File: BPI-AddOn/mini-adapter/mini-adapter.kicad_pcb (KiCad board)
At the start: 2 copper layers, 50 x 50 mm, 17 parts, among them J1 RJ45, J3 MS2 Kabel, J4 Grove, J5 RJ45, P1 DIN10-1, P2 DIN7-1, P3 CONN_01X05, P4 CAN Term

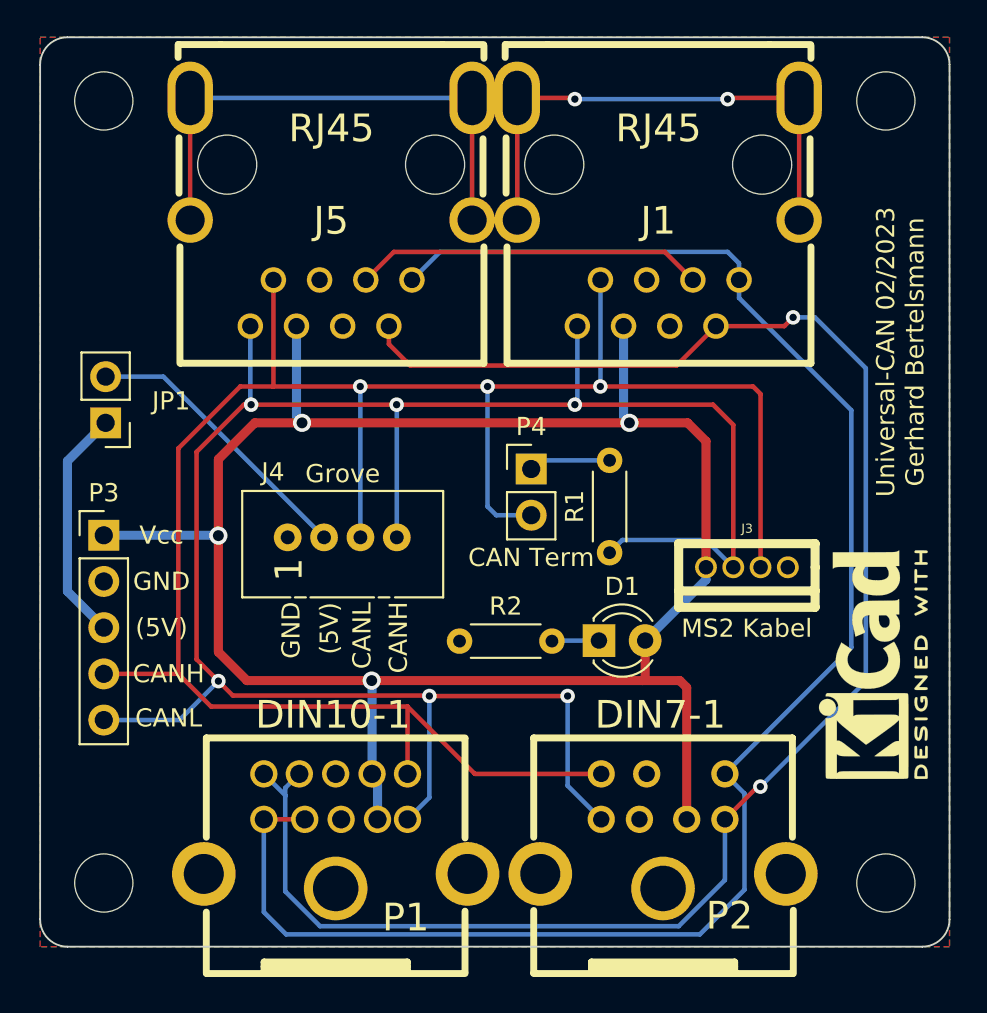
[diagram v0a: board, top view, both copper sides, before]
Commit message: add MS1 Slave / Pin 5 Vcc
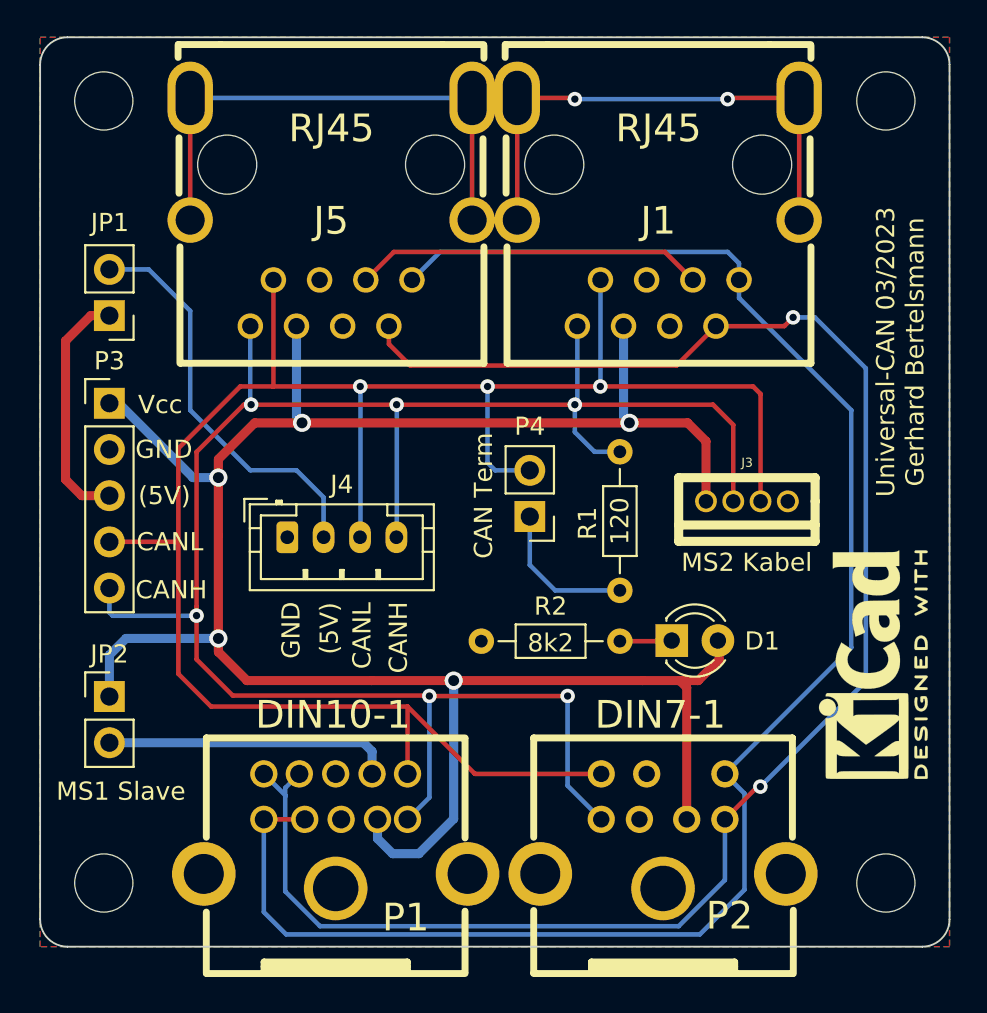
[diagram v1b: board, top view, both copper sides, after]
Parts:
- added JP2: MS1 Slave, Connector_PinHeader_2.54mm:PinHeader_1x02_P2.54mm_Vertical, F.Cu at (114.8, 111.2)
- J4: footprint Maerklin:Grove_1x04 -> Connector_JST:JST_PH_B4B-PH-K_1x04_P2.00mm_Vertical
- R1, R2: footprint Resistor_THT:R_Axial_DIN0204_L3.6mm_D1.6mm_P5.08mm_Horizontal -> Resistor_THT:R_Axial_DIN0204_L3.6mm_D1.6mm_P7.62mm_Horizontal
- moved P3 7.26 mm to (114.8, 95.1)
- moved JP1 5.90 mm to (114.8, 90.3)
- moved R1 5.58 mm to (142.9, 97.8), turned to -90 degrees
- moved D1 4.00 mm to (145.7, 108.2)
- moved J3 3.62 mm to (149.9, 100.5)
- moved P4 2.61 mm to (137.9, 101.4), turned to 180 degrees
- moved R2 1.20 mm to (135.3, 108.2)
- turned J4 to 0 degrees
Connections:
- P1 pad 5: /Vcc -> Net-(P1-Pad5)
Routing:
- net Net-(P1-Pad5): track 0.00 -> 15.9 mm
- net /Vcc: track 112.0 -> 120.7 mm, vias 4 -> 5
- net /CANH: track 117.2 -> 109.4 mm
- net Net-(J4-Pad2): track 15.7 -> 22.4 mm
- net /CANL: track 118.1 -> 111.6 mm
- net Net-(P4-Pad1): track 4.51 -> 8.19 mm
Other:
- board text added: "Universal-CAN 03/2023 Gerhard Bertelsmann"
- board text removed: "Universal-CAN 02/2023 Gerhard Bertelsmann"

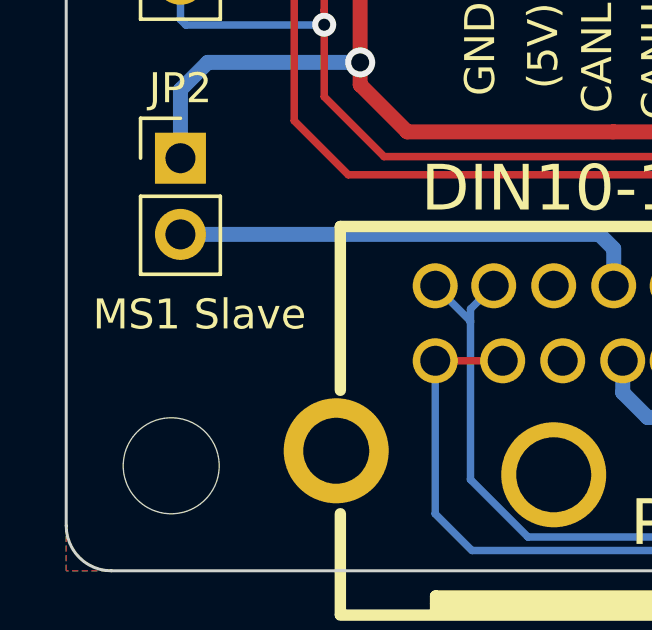
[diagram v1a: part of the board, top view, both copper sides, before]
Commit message: rename JP2 to MS1 Master
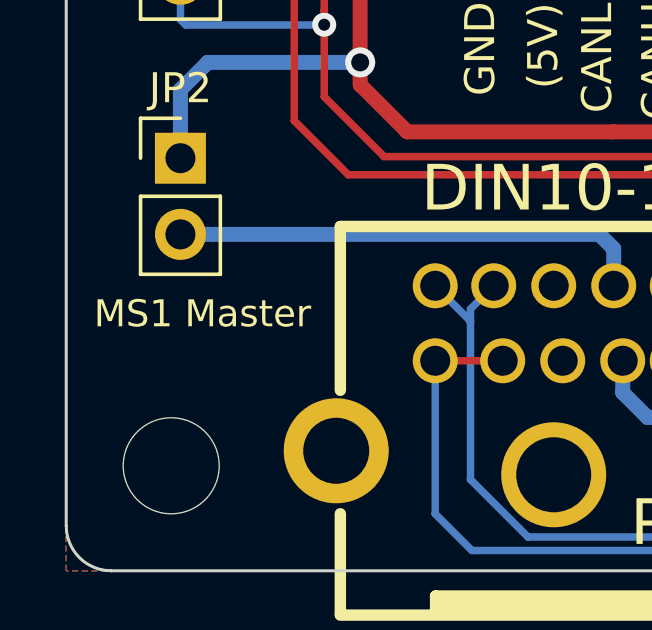
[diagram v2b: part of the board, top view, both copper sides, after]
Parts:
- JP2: value MS1 Slave -> MS1 Master
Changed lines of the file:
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@@
   (net 13 "Net-(P4-Pad1)")
   (net 14 "Net-(J1-PadSH)")
-  (net 15 "Net-(P1-Pad5)")
+  (net 15 "Net-(JP2-Pad2)")
   (footprint "Resistor_THT:R_Axial_DIN0204_L3.6mm_D1.6mm_P7.62mm_Horizontal" (layer "F.Cu")
     (at 142.875 97.79 -90)
@@
       (effects (font (size 1 1) (thickness 0.15)))
     )
-    (fp_text value "MS1 Slave" (at 0.635 5.212) (layer "F.SilkS")
-      (effects (font (size 1 1) (thickness 0.15)))
+    (fp_text value "MS1 Master" (at 0.7366 5.1866) (layer "F.SilkS")
+      (effects (font (size 0.9 0.9) (thickness 0.15)))
     )
     (fp_text user "${REFERENCE}" (at 0 1.27 90) (layer "F.Fab")
@@
       (net 2 "/Vcc") (pinfunction "A") (pintype "passive"))
     (pad "2" thru_hole oval (at 0 2.54) (size 1.7 1.7) (drill 1) (layers *.Cu *.Mask)
-      (net 15 "Net-(P1-Pad5)") (pinfunction "B") (pintype "passive"))
+      (net 15 "Net-(JP2-Pad2)") (pinfunction "B") (pintype "passive"))
     (model "${KICAD6_3DMODEL_DIR}/Connector_PinHeader_2.54mm.3dshapes/PinHeader_1x02_P2.54mm_Vertical.wrl"
       (offset (xyz 0 0 0))
@@
       (net 9 "/CANH") (pinfunction "Pin_4") (pintype "passive"))
     (pad "5" thru_hole circle (at 2 -4.5) (size 1.5 1.5) (drill 1) (layers *.Cu *.SilkS *.Mask)
-      (net 15 "Net-(P1-Pad5)") (pinfunction "Pin_5") (pintype "passive"))
+      (net 15 "Net-(JP2-Pad2)") (pinfunction "Pin_5") (pintype "passive"))
     (pad "6" thru_hole circle (at 0 -4.5) (size 1.5 1.5) (drill 1) (layers *.Cu *.SilkS *.Mask)
       (net 6 "GND") (pinfunction "Pin_6") (pintype "passive"))

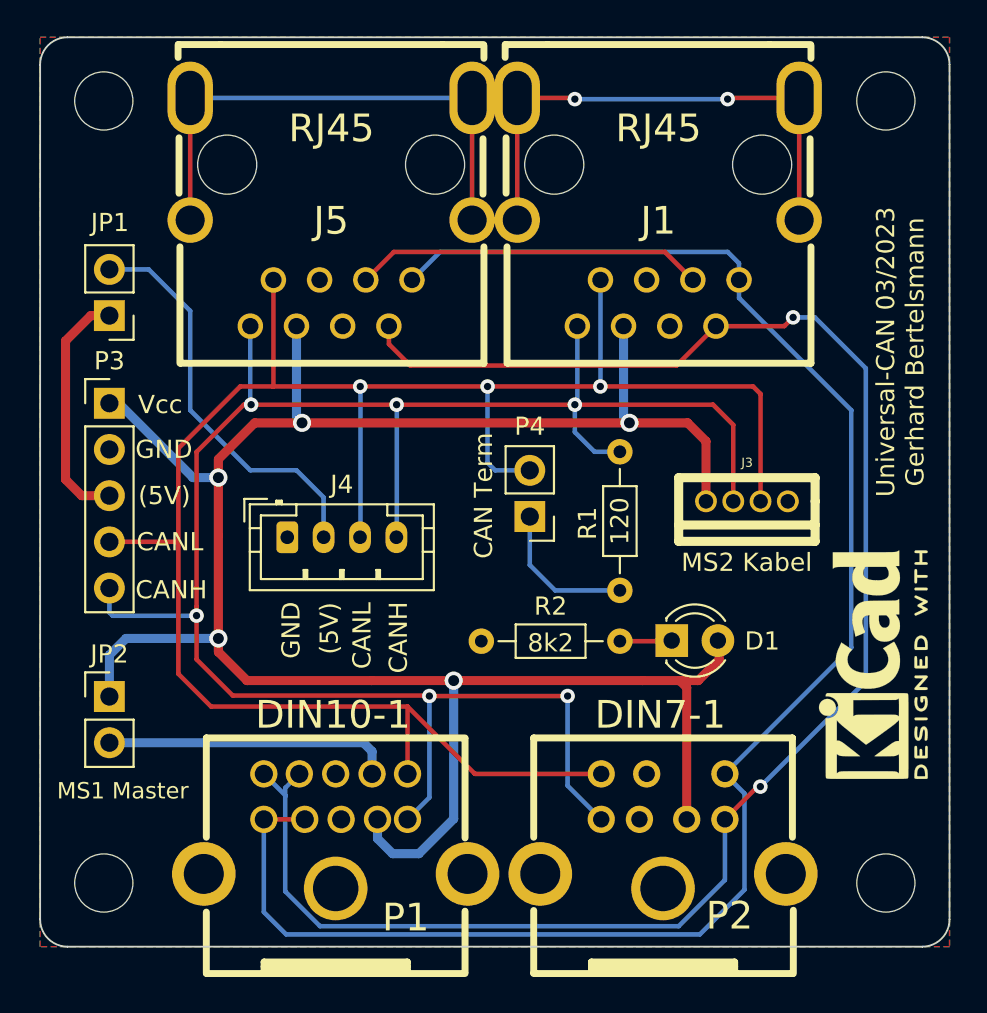
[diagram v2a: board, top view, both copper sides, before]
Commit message: move some description on the silkscreen
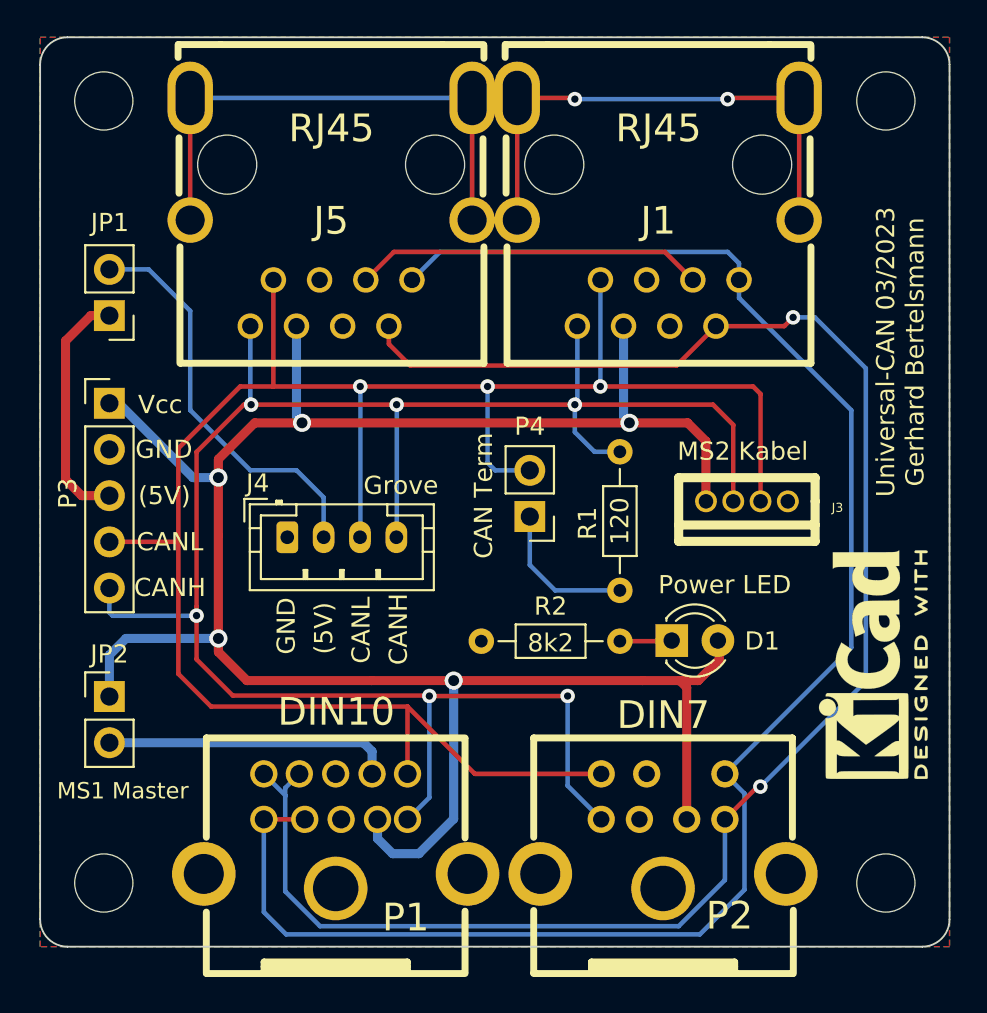
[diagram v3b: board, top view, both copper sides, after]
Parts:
- D1: value LED -> Power LED
- P1: value DIN10-1 -> DIN10
- P2: value DIN7-1 -> DIN7
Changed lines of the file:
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@@
     (property "Sheetname" "")
     (attr through_hole)
-    (fp_text reference "J4" (at 3 -2.9) (layer "F.SilkS")
+    (fp_text reference "J4" (at -1.6256 -2.9718) (layer "F.SilkS")
       (effects (font (size 1 1) (thickness 0.15)))
     )
-    (fp_text value "Grove" (at -0.508 -2.921) (layer "F.Fab")
+    (fp_text value "Grove" (at 6.2484 -2.8448) (layer "F.SilkS")
       (effects (font (size 1 1) (thickness 0.15)))
     )
@@
       (effects (font (size 1 1) (thickness 0.15)))
     )
-    (fp_text value "LED" (at 1.27 2.96) (layer "F.Fab")
+    (fp_text value "Power LED" (at 2.9158 -3.0648) (layer "F.SilkS")
       (effects (font (size 1 1) (thickness 0.15)))
     )
@@
     (property "Sheetname" "")
     (attr through_hole)
-    (fp_text reference "P3" (at 0 -2.33) (layer "F.SilkS")
+    (fp_text reference "P3" (at -2.286 4.953 90) (layer "F.SilkS")
       (effects (font (size 1 1) (thickness 0.15)))
     )
@@
       (effects (font (size 1.524 1.524) (thickness 0.3048)))
     )
-    (fp_text value "DIN7-1" (at -0.1524 -7.747) (layer "F.SilkS")
+    (fp_text value "DIN7" (at 0.0126 -7.732) (layer "F.SilkS")
       (effects (font (size 1.524 1.524) (thickness 0.3048)))
     )
@@
       (effects (font (size 1.524 1.524) (thickness 0.3048)))
     )
-    (fp_text value "DIN10-1" (at -0.1524 -7.747) (layer "F.SilkS")
+    (fp_text value "DIN10" (at 0.0294 -7.9098) (layer "F.SilkS")
       (effects (font (size 1.524 1.524) (thickness 0.3048)))
     )
@@
     (property "Sheetname" "")
     (attr through_hole)
-    (fp_text reference "J3" (at 0.01 -2.13) (layer "F.SilkS")
+    (fp_text reference "J3" (at 4.9784 0.3484) (layer "F.SilkS")
       (effects (font (size 0.5 0.5) (thickness 0.125)))
     )
-    (fp_text value "MS2 Kabel" (at -0.01 3.36) (layer "F.SilkS")
+    (fp_text value "MS2 Kabel" (at -0.2286 -2.7504) (layer "F.SilkS")
       (effects (font (size 1 1) (thickness 0.2)))
     )
@@
   (gr_arc (start 159.5 75) (mid 160.56066 75.43934) (end 161 76.5) (layer "Edge.Cuts") (width 0.1))
   (gr_arc (start 161 123.5) (mid 160.56066 124.56066) (end 159.5 125) (layer "Edge.Cuts") (width 0.1))
-  (gr_text "GND" (at 124.8 107.6 90) (layer "F.SilkS")
+  (gr_text "GND" (at 124.5362 107.3658 90) (layer "F.SilkS")
     (effects (font (size 1 1) (thickness 0.15)))
   )
-  (gr_text "CANH\n" (at 118.2116 105.3846) (layer "F.SilkS")
+  (gr_text "CANH\n" (at 118.1354 105.2576) (layer "F.SilkS")
     (effects (font (size 1 1) (thickness 0.15)))
   )
-  (gr_text "CANL" (at 128.7 107.9 90) (layer "F.SilkS")
+  (gr_text "CANL" (at 128.651 107.5944 90) (layer "F.SilkS")
     (effects (font (size 1 1) (thickness 0.15)))
   )
@@
     (effects (font (size 1 1) (thickness 0.15)))
   )
-  (gr_text "(5V)" (at 126.9 107.5 90) (layer "F.SilkS")
+  (gr_text "(5V)" (at 126.5936 107.4928 90) (layer "F.SilkS")
     (effects (font (size 1 1) (thickness 0.15)))
   )
-  (gr_text "CANH" (at 130.7 108 90) (layer "F.SilkS")
+  (gr_text "CANH" (at 130.7 107.5436 90) (layer "F.SilkS")
     (effects (font (size 1 1) (thickness 0.15)))
   )
